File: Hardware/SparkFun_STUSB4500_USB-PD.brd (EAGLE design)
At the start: 33 x 33 mm, 74 parts, among them J4 QWIIC, Q1 7.6A/30V/29mΩ, U1 STUSB4500, U2 3.3V

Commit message: v01
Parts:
- removed U$28: (no value), buzzard_labels (9):USB#PD1
- added U$26: (no value), buzzard_labels (10):#ALERT0
- U$27: device buzzard_labels (9):STUSB45000 -> buzzard_labels (10):_POWER_DELIVERY2
- U$9: device buzzard_labels (3):ALERT9 -> buzzard_labels (10):USB#C1
- moved U$27 5.29 mm to (14.7, 15.7)
- moved LOGO2 1.27 mm to (20.4, 16.5)
- moved U$9 0.74 mm to (11.0, 18.0), turned to 0 degrees
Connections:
- net ALERT renamed !ALERT
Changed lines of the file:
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@@
 <setting verticaltext="up"/>
 </settings>
-<grid distance="50" unitdist="mil" unit="inch" style="lines" multiple="1" display="no" altdistance="5" altunitdist="mil" altunit="inch"/>
+<grid distance="50" unitdist="inch" unit="inch" style="lines" multiple="1" display="yes" altdistance="5" altunitdist="mil" altunit="inch"/>
 <layers>
 <layer number="1" name="Top" color="4" fill="1" visible="yes" active="yes"/>
@@
 <layer number="22" name="bPlace" color="7" fill="1" visible="yes" active="yes"/>
 <layer number="23" name="tOrigins" color="15" fill="1" visible="yes" active="yes"/>
-<layer number="24" name="bOrigins" color="15" fill="1" visible="no" active="yes"/>
+<layer number="24" name="bOrigins" color="15" fill="1" visible="yes" active="yes"/>
 <layer number="25" name="tNames" color="7" fill="1" visible="no" active="yes"/>
 <layer number="26" name="bNames" color="7" fill="1" visible="no" active="yes"/>
@@
 <element name="U$7" library="buzzard_labels (3)" package="D#8" value="" x="6.35" y="21.844" smashed="yes" rot="MR90"/>
 <element name="U$8" library="buzzard_labels (3)" package="D#7" value="" x="8.89" y="21.717" smashed="yes" rot="MR90"/>
-<element name="U$9" library="buzzard_labels (3)" package="ALERT9" value="" x="11.43" y="18.669" smashed="yes" rot="MR90"/>
 <element name="U$10" library="buzzard_labels (3)" package="RESET10" value="" x="13.97" y="18.796" smashed="yes" rot="MR90"/>
 <element name="U$12" library="buzzard_labels (3)" package="VIN6" value="" x="1.27" y="20.955" smashed="yes" rot="MR90"/>
@@
 <element name="U$24" library="buzzard_labels (7)" package="VSNK1" value="" x="24.384" y="12.573" smashed="yes" rot="MR90"/>
 <element name="LOGO1" library="SparkFun-Aesthetics" package="OSHW-LOGO-S" value="OSHW-LOGOS" x="20.955" y="18.161" smashed="yes"/>
-<element name="LOGO2" library="SparkFun-Aesthetics" package="SFE_LOGO_NAME_.1" value="SFE_LOGO_NAME.1_INCH" x="21.717" y="16.51" smashed="yes" rot="MR90"/>
-<element name="U$27" library="buzzard_labels (9)" package="STUSB45000" value="" x="9.906" y="17.907" smashed="yes" rot="MR0"/>
-<element name="U$28" library="buzzard_labels (9)" package="USB#PD1" value="" x="8.636" y="15.367" smashed="yes" rot="MR0"/>
+<element name="LOGO2" library="SparkFun-Aesthetics" package="SFE_LOGO_NAME_.1" value="SFE_LOGO_NAME.1_INCH" x="20.447" y="16.51" smashed="yes" rot="MR90"/>
 <element name="U$25" library="SparkFun-Aesthetics" package="SFE_LOGO_FLAME_.1" value="" x="14.351" y="21.336" smashed="yes"/>
 <element name="LOGO3" library="SparkFun-Aesthetics" package="QWIIC_5MM" value="QWIIC_LOGO_5MM" x="28.575" y="9.652" smashed="yes" rot="MR0"/>
+<element name="U$26" library="buzzard_labels (10)" package="#ALERT0" value="" x="11.43" y="19.304" smashed="yes" rot="MR90"/>
+<element name="U$9" library="buzzard_labels (10)" package="USB#C1" value="" x="11.049" y="18.034" smashed="yes" rot="MR0"/>
+<element name="U$27" library="buzzard_labels (10)" package="_POWER_DELIVERY2" value="" x="14.732" y="15.748" smashed="yes" rot="MR0"/>
 </elements>
 <signals>
@@
 <via x="22.987" y="20.193" extent="1-16" drill="0.3048"/>
 </signal>
-<signal name="ALERT">
+<signal name="!ALERT">
 <contactref element="U1" pad="P$19"/>
 <wire x1="13.188" y1="18.41" x2="13.188" y2="23.622" width="0.2032" layer="1"/>

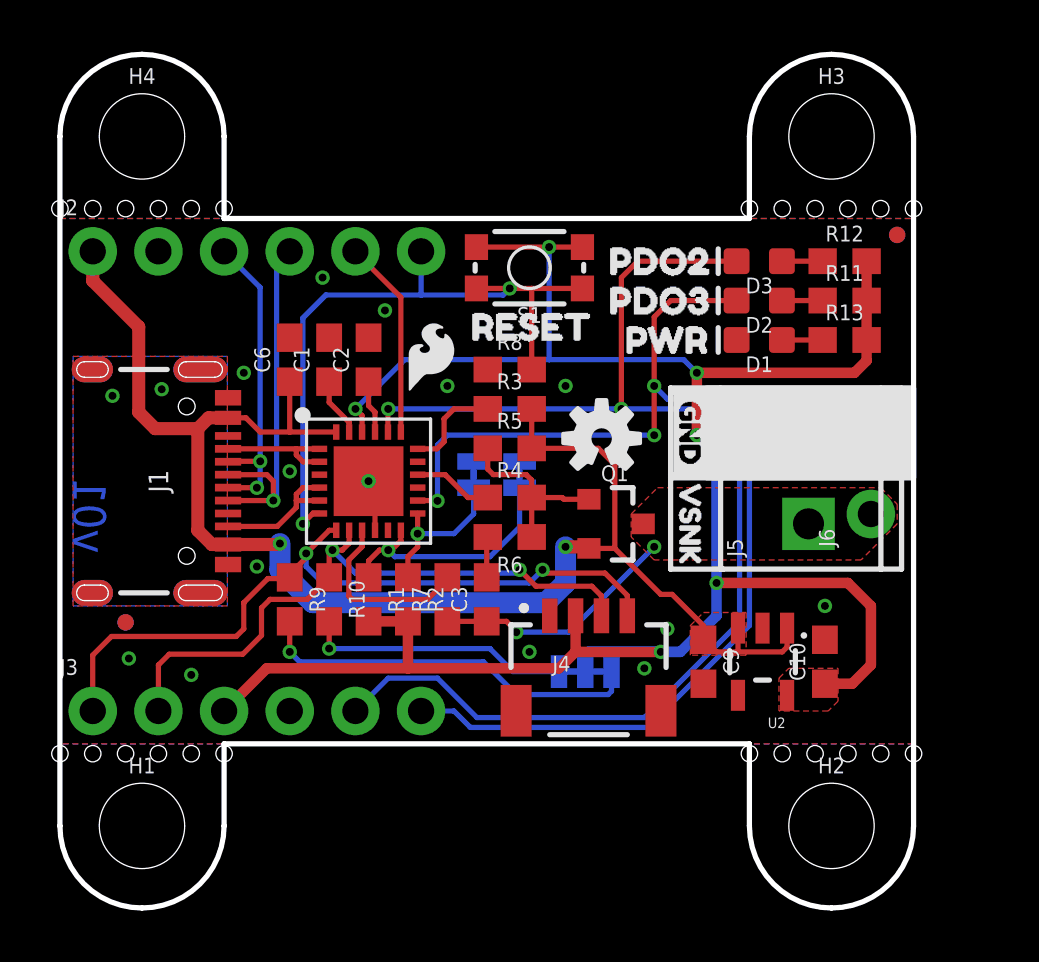
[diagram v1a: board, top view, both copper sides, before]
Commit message: v02
-Added ESD protection diodes to VIN,VSNK, CC1, CC2
-Removed 3.3V LDO and replaced with the internal 2.7V regulated output of the STUSB4500.
-Added reverse current protection to the 2.7V regulator when VDD > 2.7V
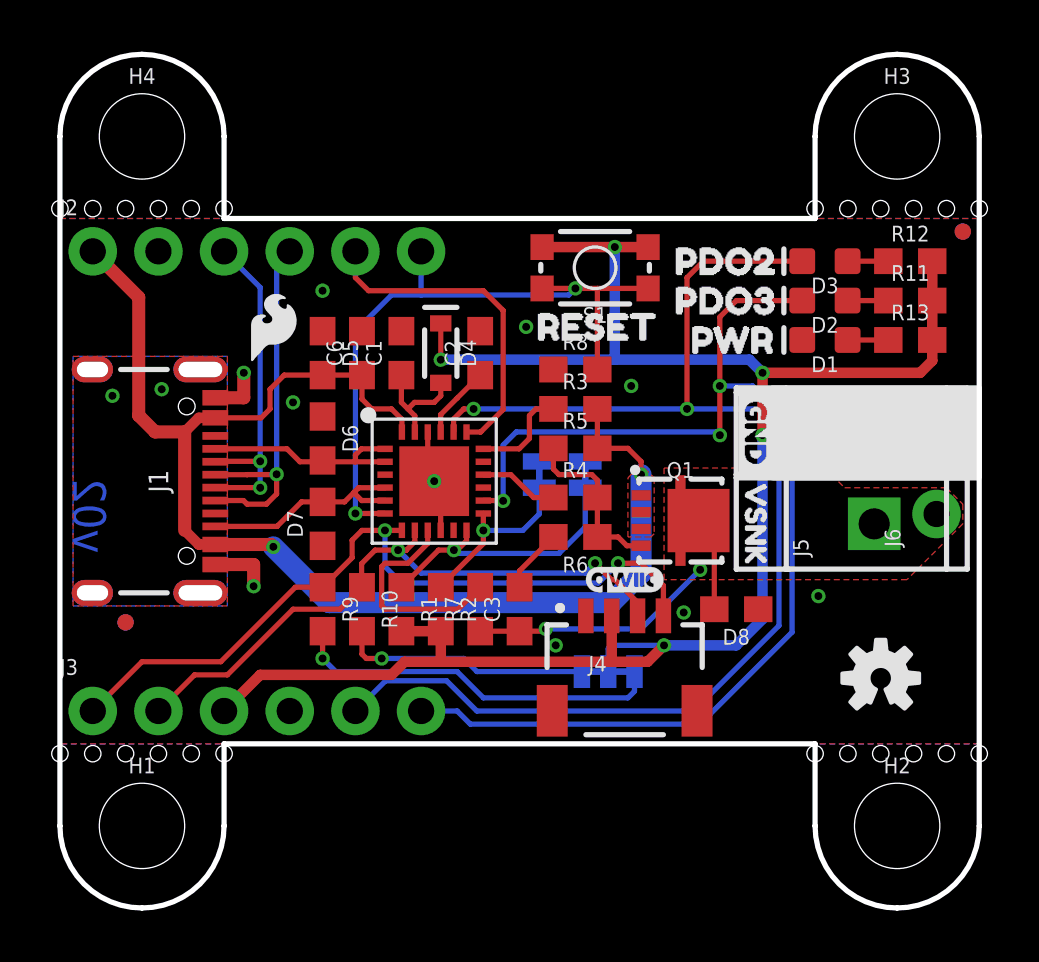
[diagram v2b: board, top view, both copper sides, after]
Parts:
- removed C10, C9: 4.7uF, SparkFun-Capacitors:0603
- removed U2: 3.3V, SparkFun-IC-Power:SOT23-5
- added D4: BAT60A, SparkFun-DiscreteSemi:SOD-323
- added D5, D6, D7, D8: 24V, SparkFun-DiscreteSemi:0603
- LOGO3: value QWIIC_LOGO_5MM -> QWIIC_LOGO_3MM; device SparkFun-Aesthetics:QWIIC_5MM -> SparkFun-Aesthetics:QWIIC_3MM
- Q1: value 7.6A/30V/29mΩ -> 9A/30V/15mΩ; device SparkFun-DiscreteSemi:SOT23-3 -> stusb4500:8-POWERVDFN-3X3
- R10, R9: value 4.7k -> 2.2k
- moved LOGO1 14.2 mm to (31.8, 8.89)
- moved LOGO3 7.39 mm to (21.8, 12.7), flipped to the top
- moved U$25 6.20 mm to (8.26, 22.5)
- moved C2 4.33 mm to (16.3, 21.5)
- moved C1 2.81 mm to (13.2, 21.5)
- moved C6 2.81 mm to (11.7, 21.5)
- moved FD2 2.54 mm to (34.9, 26.2)
- moved FD3 2.54 mm to (34.9, 26.2)
- moved Q1 2.54 mm to (24.0, 15.0)
- moved D1 2.54 mm to (29.6, 22.0)
- moved D2 2.54 mm to (29.6, 23.5)
- moved D3 2.54 mm to (29.6, 25.0)
- moved JP3 2.54 mm to (18.5, 16.8)
- moved U$16 2.54 mm to (18.5, 10.7)
- moved U$18 2.54 mm to (23.5, 22.0)
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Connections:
- removed net 3.3V: C10.1, J3.3, J4.2, JP1.2, R1.2, R11.2, R12.2, R13.2, R2.2, S1.1, S1.2, U1.P$22, U2.5
- new net VDD: D4.C, J3.3, J4.2, JP1.2, R1.2, R11.2, R12.2, R13.2, R2.2, S1.1, S1.2
- net 2.7V: now also D4.A
- net CC1: now also D6.2
- net CC2: now also D7.2
- net GND: now also D5.1, D6.1, D7.1, D8.1, U1.P$22; no longer C10.2, C9.2, U2.2
- net N$8: now also Q1.4; no longer Q1.1
- net VIN: now also D5.2, Q1.1, Q1.3; no longer C9.1, U2.1, U2.3
- net VSNK: now also D8.2, Q1.5@1, Q1.5@2, Q1.5@3; no longer Q1.3
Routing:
- net 3.3V: track 83.8 -> 0.00 mm, vias 6 -> 0
- net VDD: track 0.00 -> 72.5 mm, vias 0 -> 5
- net VIN: track 59.4 -> 51.5 mm
- net GND: track 2.00 -> 8.40 mm, vias 14 -> 10
- net !ALERT: track 7.72 -> 12.9 mm
- net VSNK: track 9.57 -> 13.2 mm
- net CC1: track 4.77 -> 8.36 mm
- net CC2: track 5.35 -> 8.53 mm
- net 2.7V: track 2.27 -> 4.40 mm
- net DISCH: track 7.02 -> 8.40 mm
- net D-: track 12.2 -> 13.2 mm
- net ADDR0: track 9.80 -> 10.7 mm
- net N$10: track 1.58 -> 2.49 mm
- net ADDR1: track 6.12 -> 6.98 mm
- net 1.2V: track 2.05 -> 2.84 mm
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- removed copper zone on layer 1, net 3.3V
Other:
- board size 33 x 33 mm -> 35.6 x 33 mm
- board text added: "v02"
- board text removed: "v01"

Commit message: v20
- Updated Labels
- Connected VSYS to VDD
- Replaced Power LED with GPIO LED
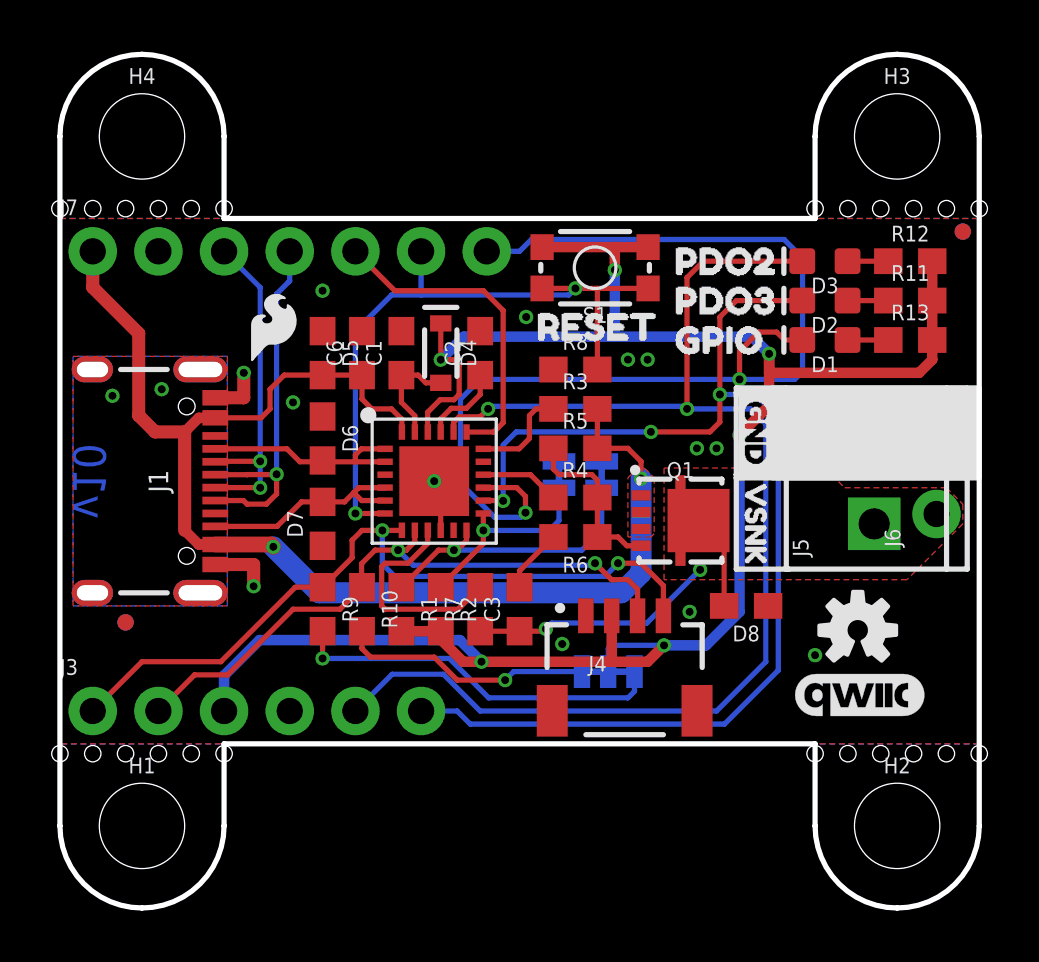
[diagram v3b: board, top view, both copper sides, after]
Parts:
- removed J2: (no value), SparkFun-Connectors:1X06_NO_SILK
- added J7: (no value), SparkFun-Connectors:1X07_NO_SILK
- added U$28: (no value), buzzard_labels:GPIO0
- D1: value RED -> BLUE
- D2: value BLUE -> Yellow
- LOGO3: value QWIIC_LOGO_3MM -> QWIIC_LOGO_5MM; device SparkFun-Aesthetics:QWIIC_3MM -> SparkFun-Aesthetics:QWIIC_5MM
- U$1: device buzzard_labels (2):3V310 -> buzzard_labels:VDD2
- U$18: device buzzard_labels (4):PWR6 -> buzzard_labels:GPIO1
- moved LOGO3 10.1 mm to (30.9, 8.26)
- moved LOGO1 2.06 mm to (30.9, 10.7)
- moved U$16 0.76 mm to (19.3, 10.7)
- moved JP3 0.76 mm to (19.3, 16.8)
- moved U$15 0.64 mm to (21.0, 10.7)
- moved U$18 0.64 mm to (22.9, 22.0)
- moved JP2 0.63 mm to (21.0, 16.8)
- moved LOGO2 0.51 mm to (23.5, 16.5)
- moved D8 0.40 mm to (26.5, 11.7)
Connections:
- new net GPIO: D1.C, J7.7, U1.P$15
- net !ALERT: now also J7.5; no longer J2.5
- net D+: now also J7.4; no longer J2.4
- net D-: now also J7.3; no longer J2.3
- net GND: now also J7.2; no longer D1.C, J2.2, U1.P$22
- net RESET: now also J7.6; no longer J2.6
- net VDD: now also U1.P$22
- net VIN: now also J7.1; no longer J2.1
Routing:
- net GPIO: track 0.00 -> 43.5 mm, vias 0 -> 2
- net VDD: track 72.5 -> 79.7 mm, vias 5 -> 6
- net GND: track 8.40 -> 6.75 mm, vias 10 -> 13
- net ADDR1: track 6.98 -> 7.89 mm
- net ADDR0: track 10.7 -> 11.4 mm
- net POWER_PDO3: track 47.1 -> 46.5 mm
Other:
- board text added: "v10"
- board text removed: "v02"

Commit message: Update SparkFun_STUSB4500_USB-PD.brd
Updated buzzard labels for PDO2 and PDO3
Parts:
- removed U$5: (no value), buzzard_labels (3):PDO212
- removed U$6: (no value), buzzard_labels (3):PDO311
- added U$29: (no value), buzzard_labels (1):#PDO20
- added U$30: (no value), buzzard_labels (1):#PDO31
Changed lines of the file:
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@@
 <layer number="43" name="vRestrict" color="2" fill="10" visible="no" active="yes"/>
 <layer number="44" name="Drills" color="7" fill="1" visible="no" active="yes"/>
-<layer number="45" name="Holes" color="7" fill="1" visible="yes" active="yes"/>
+<layer number="45" name="Holes" color="7" fill="1" visible="no" active="yes"/>
 <layer number="46" name="Milling" color="3" fill="1" visible="no" active="yes"/>
-<layer number="47" name="Measures" color="7" fill="1" visible="no" active="yes"/>
+<layer number="47" name="Measures" color="7" fill="1" visible="yes" active="yes"/>
 <layer number="48" name="Document" color="7" fill="1" visible="no" active="yes"/>
 <layer number="49" name="Reference" color="7" fill="1" visible="no" active="yes"/>
 <layer number="50" name="dxf" color="7" fill="1" visible="no" active="yes"/>
 <layer number="51" name="tDocu" color="6" fill="1" visible="yes" active="yes"/>
-<layer number="52" name="bDocu" color="7" fill="1" visible="no" active="yes"/>
+<layer number="52" name="bDocu" color="7" fill="1" visible="yes" active="yes"/>
 <layer number="91" name="Nets" color="2" fill="1" visible="no" active="no"/>
 <layer number="92" name="Busses" color="1" fill="1" visible="no" active="no"/>
@@
 <element name="U$4" library="buzzard_labels (2)" package="SCL12" value="" x="1.27" y="7.874" smashed="yes" rot="MR90"/>
 <element name="U$11" library="buzzard_labels (2)" package="GND6" value="" x="3.81" y="20.447" smashed="yes" rot="MR90"/>
-<element name="U$5" library="buzzard_labels (3)" package="PDO212" value="" x="11.43" y="7.874" smashed="yes" rot="MR90"/>
-<element name="U$6" library="buzzard_labels (3)" package="PDO311" value="" x="13.97" y="7.874" smashed="yes" rot="MR90"/>
 <element name="U$7" library="buzzard_labels (3)" package="D#8" value="" x="6.35" y="21.844" smashed="yes" rot="MR90"/>
 <element name="U$8" library="buzzard_labels (3)" package="D#7" value="" x="8.89" y="21.717" smashed="yes" rot="MR90"/>
@@
 <element name="U$1" library="buzzard_labels" package="VDD2" value="" x="6.35" y="7.874" smashed="yes" rot="MR90"/>
 <element name="U$18" library="buzzard_labels" package="GPIO1" value="" x="22.86" y="21.971" smashed="yes"/>
+<element name="U$29" library="buzzard_labels (1)" package="#PDO20" value="" x="11.43" y="7.747" smashed="yes" rot="MR90"/>
+<element name="U$30" library="buzzard_labels (1)" package="#PDO31" value="" x="13.97" y="7.747" smashed="yes" rot="MR90"/>
 </elements>
 <signals>

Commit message: v10
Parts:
- Q1: device stusb4500:8-POWERVDFN-3X3 -> SparkFun-DiscreteSemi:8-POWERVDFN-3X3
- moved U$9 3.32 mm to (13.9, 14.7)
- moved U$27 2.43 mm to (17.0, 18.2)
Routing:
- net GPIO: track 43.5 -> 29.3 mm, vias 2 -> 3
- net RESET: track 26.3 -> 26.9 mm

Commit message: v10 Update
Replaced GPIO buzzard label with active low indicator
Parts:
- removed U$28: (no value), buzzard_labels:GPIO0
- added U$5: (no value), buzzard_labels (3):#GPIO0
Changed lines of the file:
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@@
 <drawing>
 <settings>
-<setting alwaysvectorfont="no"/>
+<setting alwaysvectorfont="yes"/>
 <setting verticaltext="up"/>
 </settings>
@@
 <layer number="37" name="tTest" color="7" fill="1" visible="no" active="yes"/>
 <layer number="38" name="bTest" color="7" fill="1" visible="no" active="yes"/>
-<layer number="39" name="tKeepout" color="4" fill="11" visible="yes" active="yes"/>
-<layer number="40" name="bKeepout" color="1" fill="11" visible="yes" active="yes"/>
+<layer number="39" name="tKeepout" color="4" fill="11" visible="no" active="yes"/>
+<layer number="40" name="bKeepout" color="1" fill="11" visible="no" active="yes"/>
 <layer number="41" name="tRestrict" color="4" fill="10" visible="no" active="yes"/>
 <layer number="42" name="bRestrict" color="1" fill="10" visible="no" active="yes"/>
@@
 <attribute name="VALUE" x="0" y="23.368" size="0.6096" layer="27" font="vector" ratio="20"/>
 </element>
-<element name="U$28" library="buzzard_labels" package="GPIO0" value="" x="16.51" y="19.939" smashed="yes" rot="MR90"/>
 <element name="U$1" library="buzzard_labels" package="VDD2" value="" x="6.35" y="7.874" smashed="yes" rot="MR90"/>
 <element name="U$18" library="buzzard_labels" package="GPIO1" value="" x="22.86" y="21.971" smashed="yes"/>
 <element name="U$29" library="buzzard_labels (1)" package="#PDO20" value="" x="11.43" y="7.747" smashed="yes" rot="MR90"/>
 <element name="U$30" library="buzzard_labels (1)" package="#PDO31" value="" x="13.97" y="7.747" smashed="yes" rot="MR90"/>
+<element name="U$5" library="buzzard_labels (3)" package="#GPIO0" value="" x="16.51" y="20.4216" smashed="yes" rot="MR90"/>
 </elements>
 <signals>
